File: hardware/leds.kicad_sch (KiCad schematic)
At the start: 51 parts

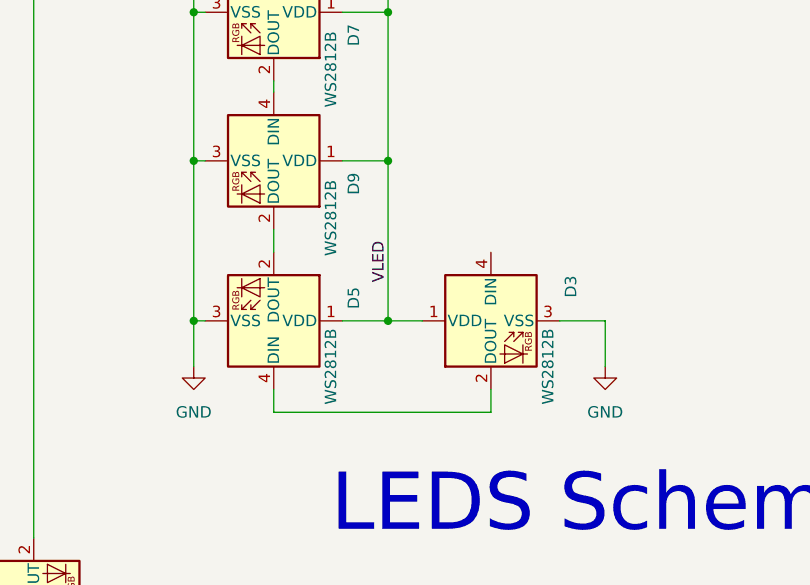
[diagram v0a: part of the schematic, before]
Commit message: Firmware is close. We just need to add the flags, test one more time, and add back the lowpower stuff that messes with rshell.
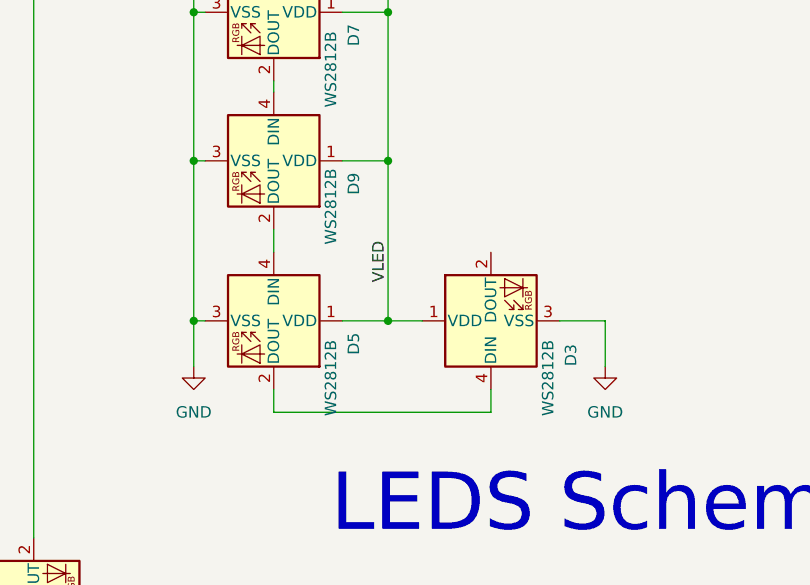
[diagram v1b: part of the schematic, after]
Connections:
- net at D5.2 (DOUT): now also D3.4 (DIN); no longer D9.2 (DOUT)
- net at D5.4 (DIN): now also D9.2 (DOUT); no longer D3.2 (DOUT)
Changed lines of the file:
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@@
+    (stroke (width 0) (type default))
+  )
+  (wire (pts (xy 186.69 163.83) (xy 210.82 163.83))
     (stroke (width 0) (type default))
   )
@@
   )
   (wire (pts (xy 120.65 135.89) (xy 121.92 135.89))
-    (stroke (width 0) (type default))
-  )
-  (wire (pts (xy 186.69 163.83) (xy 210.82 163.83))
     (stroke (width 0) (type default))
   )
@@
     )
   )
-  (symbol (lib_id "LED:WS2812B") (at 186.69 153.67 270) (mirror x) (unit 1)
-    (in_bom yes) (on_board yes) (dnp no)
-    (property "Reference" "D5" (at 195.58 151.13 0)
-      (effects (font (size 1.27 1.27)))
-    )
-    (property "Value" "WS2812B" (at 193.04 158.75 0)
-      (effects (font (size 1.27 1.27)))
-    )
-    (property "Footprint" "LED_SMD:LED_WS2812B_PLCC4_5.0x5.0mm_P3.2mm" (at 179.07 152.4 0)
-      (effects (font (size 1.27 1.27)) (justify left top) hide)
-    )
-    (property "Datasheet" "https://www.aliexpress.us/item/2255801159561004.html?spm=a2g0o.ppclist.product.2.30bfKwflKwflRx&pdp_npi=2%40dis%21USD%21%241.38%21%240.98%21%21%21%21%21%402103146c16873547621273886efcbf%2110000015757518615%21btf&_t=pvid%3A4bc5a975-9ddb-4fc8-b332-dc41c34648df&afTraceInfo=4001345875756__pc__pcBridgePPC__xxxxxx__1687354762&gatewayAdapt=glo2usa4itemAdapt" (at 177.165 151.13 0)
+  (symbol (lib_id "LED:WS2812B") (at 186.69 153.67 270) (unit 1)
+    (in_bom yes) (on_board yes) (dnp no)
+    (property "Reference" "D5" (at 195.58 156.21 0)
+      (effects (font (size 1.27 1.27)))
+    )
+    (property "Value" "WS2812B" (at 193.04 160.02 0)
+      (effects (font (size 1.27 1.27)))
+    )
+    (property "Footprint" "LED_SMD:LED_WS2812B_PLCC4_5.0x5.0mm_P3.2mm" (at 179.07 154.94 0)
+      (effects (font (size 1.27 1.27)) (justify left top) hide)
+    )
+    (property "Datasheet" "https://www.aliexpress.us/item/2255801159561004.html?spm=a2g0o.ppclist.product.2.30bfKwflKwflRx&pdp_npi=2%40dis%21USD%21%241.38%21%240.98%21%21%21%21%21%402103146c16873547621273886efcbf%2110000015757518615%21btf&_t=pvid%3A4bc5a975-9ddb-4fc8-b332-dc41c34648df&afTraceInfo=4001345875756__pc__pcBridgePPC__xxxxxx__1687354762&gatewayAdapt=glo2usa4itemAdapt" (at 177.165 156.21 0)
       (effects (font (size 1.27 1.27)) (justify left top) hide)
     )
@@
     )
   )
-  (symbol (lib_id "LED:WS2812B") (at 210.82 153.67 90) (mirror x) (unit 1)
-    (in_bom yes) (on_board yes) (dnp no)
-    (property "Reference" "D3" (at 219.71 149.86 0)
-      (effects (font (size 1.27 1.27)))
-    )
-    (property "Value" "WS2812B" (at 217.17 158.75 0)
-      (effects (font (size 1.27 1.27)))
-    )
-    (property "Footprint" "LED_SMD:LED_WS2812B_PLCC4_5.0x5.0mm_P3.2mm" (at 218.44 154.94 0)
-      (effects (font (size 1.27 1.27)) (justify left top) hide)
-    )
-    (property "Datasheet" "https://www.aliexpress.us/item/2255801159561004.html?spm=a2g0o.ppclist.product.2.30bfKwflKwflRx&pdp_npi=2%40dis%21USD%21%241.38%21%240.98%21%21%21%21%21%402103146c16873547621273886efcbf%2110000015757518615%21btf&_t=pvid%3A4bc5a975-9ddb-4fc8-b332-dc41c34648df&afTraceInfo=4001345875756__pc__pcBridgePPC__xxxxxx__1687354762&gatewayAdapt=glo2usa4itemAdapt" (at 220.345 156.21 0)
+  (symbol (lib_id "LED:WS2812B") (at 210.82 153.67 90) (unit 1)
+    (in_bom yes) (on_board yes) (dnp no)
+    (property "Reference" "D3" (at 219.71 157.48 0)
+      (effects (font (size 1.27 1.27)))
+    )
+    (property "Value" "WS2812B" (at 217.17 160.02 0)
+      (effects (font (size 1.27 1.27)))
+    )
+    (property "Footprint" "LED_SMD:LED_WS2812B_PLCC4_5.0x5.0mm_P3.2mm" (at 218.44 152.4 0)
+      (effects (font (size 1.27 1.27)) (justify left top) hide)
+    )
+    (property "Datasheet" "https://www.aliexpress.us/item/2255801159561004.html?spm=a2g0o.ppclist.product.2.30bfKwflKwflRx&pdp_npi=2%40dis%21USD%21%241.38%21%240.98%21%21%21%21%21%402103146c16873547621273886efcbf%2110000015757518615%21btf&_t=pvid%3A4bc5a975-9ddb-4fc8-b332-dc41c34648df&afTraceInfo=4001345875756__pc__pcBridgePPC__xxxxxx__1687354762&gatewayAdapt=glo2usa4itemAdapt" (at 220.345 151.13 0)
       (effects (font (size 1.27 1.27)) (justify left top) hide)
     )
@@
       (effects (font (size 1.27 1.27)))
     )
-    (property "Value" "WS2812B" (at 193.04 142.24 0)
-      (effects (font (size 1.27 1.27)))
-    )
+    (property "Value" "WS2812B" (at 193.04 140.97 0)
+      (effects (font (size 1.27 1.27)))
+    )
